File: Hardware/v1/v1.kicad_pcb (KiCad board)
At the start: 2 copper layers, 104 parts, among them J1 BAT_CONN, J10 DACS, J11 SERV_0, J12 SERV_1, J13 SERV_2, J14 SERV_3, J15 SERV_4, J16 SERV_5, J17 SERV_6, J18 SERV_7, J19 CAN, J2 EN_BAT_VIN, J20 USB_B_Mini, J21 SERV_8, J22 SERV_9, J23 SERV_10, J24 SERV_11, J3 USB_A_PWR_OUTPUT, J4 GPIO1, J5 GPIO2, J6 GPIO3, J7 GPIO4, J8 GPIO5, J9 GPIO6, P1 SWD, Q1 DMN62D0UW-7, SW1 MCU_USB_POWER, SW2 BOOT0, U1 TPS54561DPRR, U2 MCP16311MS, U3 PDS760-13, U4 BMI160, U5 STM32F405RGTx, U6 TJA1051TK-3, Y1 8Mhz

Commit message: saving
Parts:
- C15, C17, C18, C6, C7: moved to B.Cu
- moved L1 93.1 mm to (167.4, 100.8), turned to -90 degrees
- moved C8 91.8 mm to (189.3, 82.2), turned to -90 degrees
- moved L2 87.6 mm to (180.3, 94.0), turned to -90 degrees
- moved C10 86.5 mm to (169.4, 105.4), turned to 90 degrees
- moved C4 85.9 mm to (191.5, 82.2), turned to -90 degrees
- moved R7 83.8 mm to (173.7, 79.9), turned to -90 degrees
- moved C6 81.3 mm to (191.5, 82.2), turned to -90 degrees
- moved C14 79.8 mm to (170.4, 94.7)
- moved C7 78.6 mm to (189.3, 82.2), turned to -90 degrees
- moved U2 77.9 mm to (173.7, 104.9), turned to 180 degrees
- moved C11 76.5 mm to (177.6, 79.9), turned to -90 degrees
- moved C9 75.6 mm to (170.3, 97.2)
- moved R3 74.1 mm to (175.8, 108.4), turned to 90 degrees
- moved U3 72.3 mm to (181.1, 84.7), turned to 180 degrees
- moved R2 70.2 mm to (177.3, 108.4), turned to -90 degrees
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
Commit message: ANITRONBO V1_0
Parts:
- C12, C26, C30, C31, R14, R15, R16, R17, R18, R19, R20, R21, R23, R24, R25, R26, SW2: moved to B.Cu
- moved H1 216.6 mm to (210.9, 73.0)
- moved H2 202.4 mm to (210.9, 115.0)
- moved H3 150.9 mm to (138.0, 73.0)
- moved SW2 143.1 mm to (177.3, 71.0)
- moved P1 135.3 mm to (147.1, 104.4), turned to 180 degrees
- moved H4 129.7 mm to (138.0, 115.0)
- moved J4 128.4 mm to (158.3, 110.5), turned to -90 degrees
- moved C20 122.1 mm to (149.3, 93.3)
- moved C26 121.3 mm to (156.1, 89.9), turned to -90 degrees
- moved C33 120.3 mm to (152.6, 85.3), turned to 90 degrees
- moved J5 119.6 mm to (152.7, 110.5), turned to -90 degrees
- moved C23 119.6 mm to (149.3, 86.1), turned to 180 degrees
- moved Y1 119.5 mm to (149.3, 89.7), turned to -90 degrees
- moved D2 116.3 mm to (160.9, 78.0), turned to -90 degrees
- moved U5 116.0 mm to (159.2, 91.5)
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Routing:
- net GND: track 0.00 -> 581.5 mm, vias 0 -> 104
- net +5V: track 0.00 -> 304.0 mm, vias 0 -> 59
- net VCC: track 0.00 -> 184.2 mm, vias 0 -> 11
- net /MCU/GP8: track 0.00 -> 50.3 mm, vias 0 -> 1
- net /MCU/SERV12: track 0.00 -> 49.5 mm, vias 0 -> 1
- net /MCU/GP9: track 0.00 -> 48.3 mm, vias 0 -> 4
- net /MCU/SERV11: track 0.00 -> 45.9 mm, vias 0 -> 1
- net /MCU/SERV8: track 0.00 -> 45.2 mm, vias 0 -> 1
- net /MCU/GP7: track 0.00 -> 44.6 mm, vias 0 -> 1
- net VOLT_METER: track 0.00 -> 44.1 mm, vias 0 -> 3
- net SWCLK: track 0.00 -> 43.6 mm, vias 0 -> 2
- net /MCU/SERV9: track 0.00 -> 42.9 mm, vias 0 -> 1
- net /MCU/SERV7: track 0.00 -> 42.4 mm, vias 0 -> 1
- net /MCU/SERV10: track 0.00 -> 42.2 mm, vias 0 -> 1
- net BAT_VIN: track 0.00 -> 41.3 mm
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- added copper zone on B.Cu, net +5V
- added copper zone on F.Cu, net +5V
- added copper zone on In1.Cu, net +5V
- added copper zone on In2.Cu, net +5V
- added copper zone on B.Cu, net BAT_VIN
- added copper zone on F.Cu, net BAT_VIN
- added copper zone on In1.Cu, net BAT_VIN
- added copper zone on In2.Cu, net BAT_VIN
- added copper zone on B.Cu, net GND
- added copper zone on F.Cu, net GND
- added copper zone on In1.Cu, net GND
- added copper zone on In2.Cu, net GND
- added copper zone on F.Cu, net SW
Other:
- board outline added: 81 x 50 mm
- copper layers 2 -> 4
- rule pad_to_mask_clearance: 0.051 -> 0.01
- rule solder_mask_min_width: 0.25 -> 0.025
- rule trace_min: 0.2 -> 0.18
- board text added: "ANITRONBO V1.0"
- board text added: "BOOTLOADER"
- board text added: "DACS"
- board text added: "GPIO"
- board text added: "Noemi Svensson Joel Svensson (2020-01)"
- board text added: "SERVOS"
- board text added: "USB PWR"

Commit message: doneish
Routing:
- net GND: track 581.5 -> 720.5 mm, vias 104 -> 129
- net VCC: track 184.2 -> 210.7 mm, vias 11 -> 12
- added copper zone on F.Cu, net VCC
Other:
- board text added: "10"
- board text added: "11"
- board text added: "12"
- board text added: "13"
- board text added: "14"
- board text added: "15"
- board text added: "16"
- board text added: "17"
- board text added: "18"
- board text added: "5V"
- board text added: "DAC"
- board text added: "FREDDY"
- board text added: "FREDDY V1.0"
- board text added: "GND"
- board text added: "GP1"
- board text added: "GP2"
- board text added: "GP3"
- board text added: "GP4"
- board text added: "GP5"
- board text added: "GP6"
- board text added: "GP7"
- board text added: "GP8"
- board text added: "GP9"
- board text added: "NRST"
- board text added: "S"
- board text added: "SWCLK"
- board text added: "SWDIO"
- board text added: "V+"
- board text added: "VCC"
- board text removed: "ANITRONBO V1.0"

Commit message: tweaks and simplification
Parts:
- removed J21: SERV_8, Connector_PinHeader_2.54mm:PinHeader_1x03_P2.54mm_Vertical
- removed J22: SERV_9, Connector_PinHeader_2.54mm:PinHeader_1x03_P2.54mm_Vertical
- removed J23: SERV_10, Connector_PinHeader_2.54mm:PinHeader_1x03_P2.54mm_Vertical
- removed J24: SERV_11, Connector_PinHeader_2.54mm:PinHeader_1x03_P2.54mm_Vertical
- removed J7: GPIO4, Connector_JST:JST_PH_B4B-PH-K_1x04_P2.00mm_Vertical
- removed J8: GPIO5, Connector_JST:JST_PH_B4B-PH-K_1x04_P2.00mm_Vertical
- removed J9: GPIO6, Connector_JST:JST_PH_B4B-PH-K_1x04_P2.00mm_Vertical
- removed R23, R24, R25, R26: 220R, Resistor_SMD:R_0603_1608Metric
- C30: moved to F.Cu
- moved J6 23.5 mm to (143.2, 87.3), turned to 180 degrees
- moved C22 21.9 mm to (141.0, 108.4), turned to 180 degrees
- moved J5 20.7 mm to (143.2, 92.1), turned to 180 degrees
- moved J4 20.3 mm to (143.2, 97.0), turned to 180 degrees
- moved C21 19.4 mm to (140.3, 105.5), turned to -90 degrees
- moved U4 17.1 mm to (142.8, 105.7), turned to -90 degrees
- moved J15 16.0 mm to (193.5, 112.0)
- moved J16 16.0 mm to (197.0, 112.0)
- moved J17 16.0 mm to (200.5, 112.0)
- moved J18 16.0 mm to (204.0, 112.0)
- moved R18 16.0 mm to (193.5, 109.1)
- moved R19 16.0 mm to (197.0, 109.1)
- moved R20 16.0 mm to (200.5, 109.1)
- moved R21 16.0 mm to (204.0, 109.1)
- moved P1 14.4 mm to (157.5, 114.3)
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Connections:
- U5 pad 24: /MCU/GP13 -> Net-(U5-Pad24)
- U5 pad 25: /MCU/GP14 -> IMU_INT2
- U5 pad 33: /MCU/GP10 -> Net-(U5-Pad33)
- U5 pad 34: /MCU/GP11 -> Net-(U5-Pad34)
- U5 pad 35: /MCU/GP12 -> Net-(U5-Pad35)
- U5 pad 36: /MCU/GP18 -> Net-(U5-Pad36)
- U5 pad 37: /MCU/SERV9 -> Net-(U5-Pad37)
- U5 pad 38: /MCU/SERV10 -> Net-(U5-Pad38)
- U5 pad 39: /MCU/SERV11 -> Net-(U5-Pad39)
- U5 pad 4: /MCU/GP15 -> Net-(U5-Pad4)
- U5 pad 40: /MCU/SERV12 -> Net-(U5-Pad40)
- U5 pad 57: IMU_INT2 -> Net-(U5-Pad57)
- U5 pad 58: /MCU/GP16 -> Net-(U5-Pad58)
- U5 pad 59: /MCU/GP17 -> Net-(U5-Pad59)
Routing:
- net /MCU/SERV12: track 49.5 -> 0.00 mm, vias 1 -> 0
- net /MCU/SERV11: track 45.9 -> 0.00 mm, vias 1 -> 0
- net /MCU/SERV9: track 42.9 -> 0.00 mm, vias 1 -> 0
- net /MCU/SERV10: track 42.2 -> 0.00 mm, vias 1 -> 0
- net /MCU/GP12: track 32.8 -> 0.00 mm, vias 2 -> 0
- net /MCU/GP11: track 31.6 -> 0.00 mm, vias 2 -> 0
- net /MCU/GP18: track 30.7 -> 0.00 mm, vias 1 -> 0
- net /MCU/GP15: track 30.1 -> 0.00 mm, vias 1 -> 0
- net /MCU/GP10: track 28.4 -> 0.00 mm, vias 1 -> 0
- net /MCU/GP14: track 24.9 -> 0.00 mm, vias 1 -> 0
- net /MCU/GP17: track 23.2 -> 0.00 mm, vias 1 -> 0
- net GND: track 720.5 -> 697.6 mm, vias 129 -> 134
- net /MCU/GP13: track 21.3 -> 0.00 mm, vias 1 -> 0
- net /MCU/GP16: track 20.4 -> 0.00 mm, vias 1 -> 0
- net /MCU/GP8: track 50.3 -> 30.0 mm, vias 1 -> 0
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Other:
- board text added: "1"
- board text added: "2"
- board text added: "3"
- board text added: "4"
- board text added: "5"
- board text added: "6"
- board text added: "7"
- board text added: "8"
- board text added: "9"
- board text removed: "10"
- board text removed: "11"
- board text removed: "12"
- board text removed: "13"
- board text removed: "14"
- board text removed: "15"
- board text removed: "16"
- board text removed: "17"
- board text removed: "18"
- board text removed: "GP1"
- board text removed: "GP2"
- board text removed: "GP3"
- board text removed: "GP4"
- board text removed: "GP5"
- board text removed: "GP6"
- board text removed: "GP7"
- board text removed: "GP8"
- board text removed: "GP9"

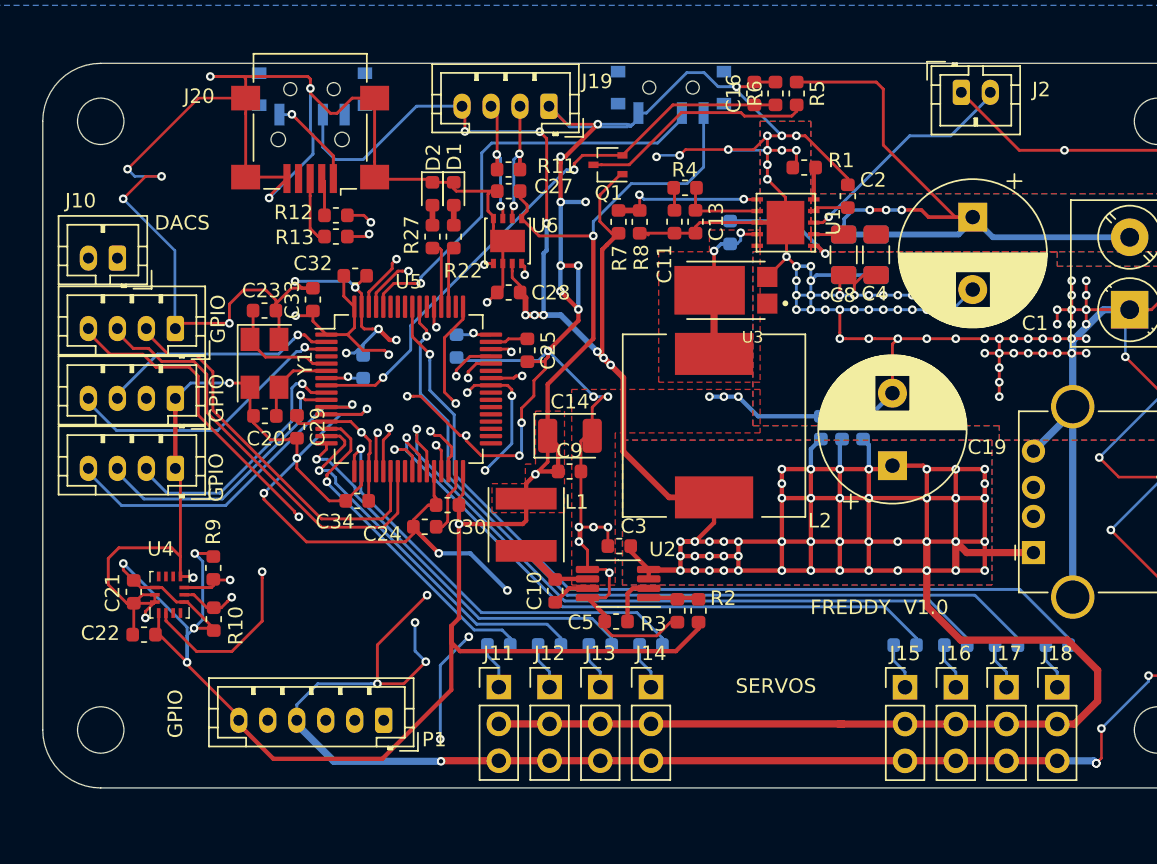
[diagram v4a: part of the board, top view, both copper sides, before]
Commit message: adding some descriptions on F silks
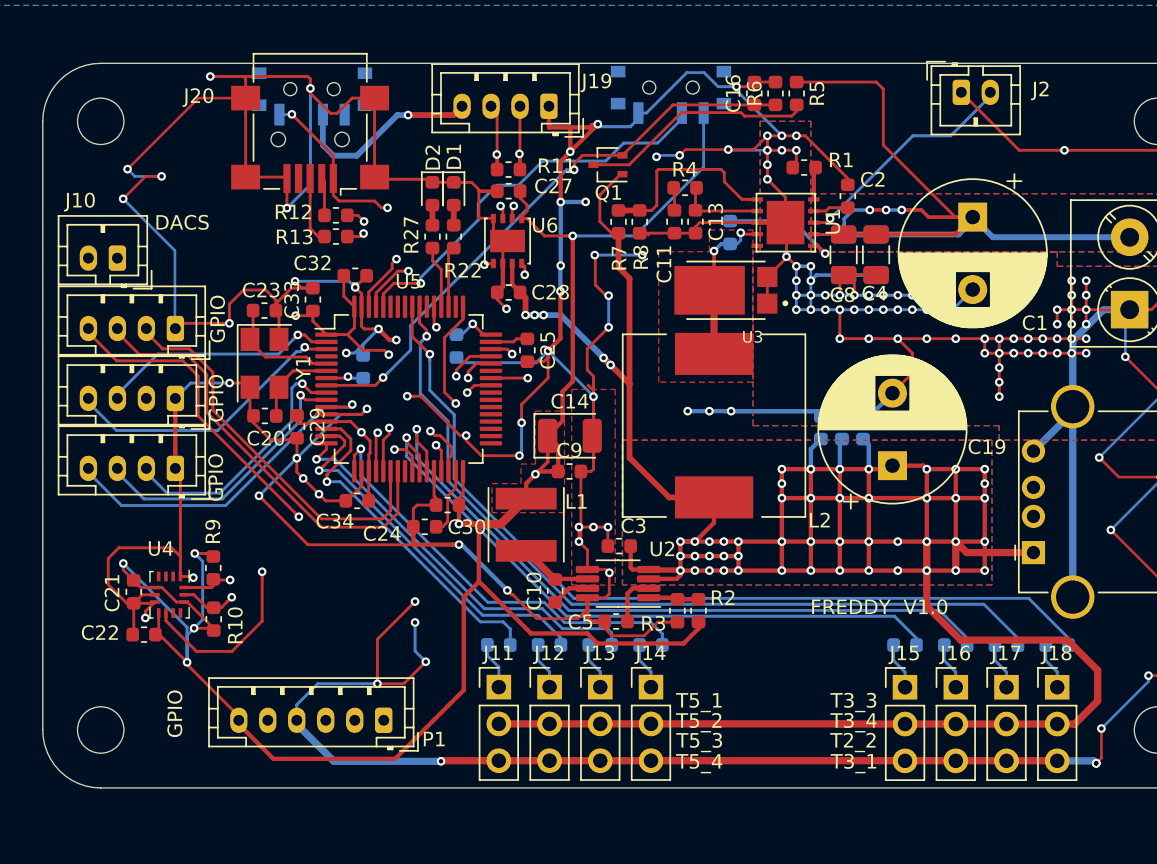
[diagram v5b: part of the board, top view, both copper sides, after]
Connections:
- U5 pad 42: +5V -> MCU_USB_VBUS
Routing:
- net GND: track 697.6 -> 726.7 mm, vias 134 -> 137
- net /MCU/GP9: track 66.4 -> 38.7 mm, vias 6 -> 2
- net MCU_USB_VBUS: track 6.48 -> 30.6 mm, vias 1 -> 3
- net BAT_VIN: track 51.7 -> 61.4 mm
- net +5V: track 303.6 -> 297.1 mm, vias 57 -> 53
- net FB: track 10.8 -> 13.3 mm, vias 2 -> 0
- net VCC: track 198.5 -> 196.1 mm
- net Net-(SW2-Pad2): track 29.7 -> 27.8 mm
- net /MCU/SERV4: track 30.2 -> 29.7 mm
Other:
- board text added: "T2_2"
- board text added: "T3_1"
- board text added: "T3_3"
- board text added: "T3_4"
- board text added: "T5_1"
- board text added: "T5_2"
- board text added: "T5_3"
- board text added: "T5_4"
- board text removed: "SERVOS"
